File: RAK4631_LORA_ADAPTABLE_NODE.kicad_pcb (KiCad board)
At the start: 2 copper layers, 75 x 49 mm, 20 parts, among them J1 Screw_Terminal_01x03, J10 Conn_01x09_Male, J11 Conn_01x09_Male, J12 Conn_01x09_Male, J14 FBB04004-M40S1003K6M, J2 Screw_Terminal_01x03, J3 Conn_01x03_Male, J4 Conn_01x03_Male, J5 Conn_01x11_Male, J8 Conn_01x11_Male, J9 Conn_01x01_Male

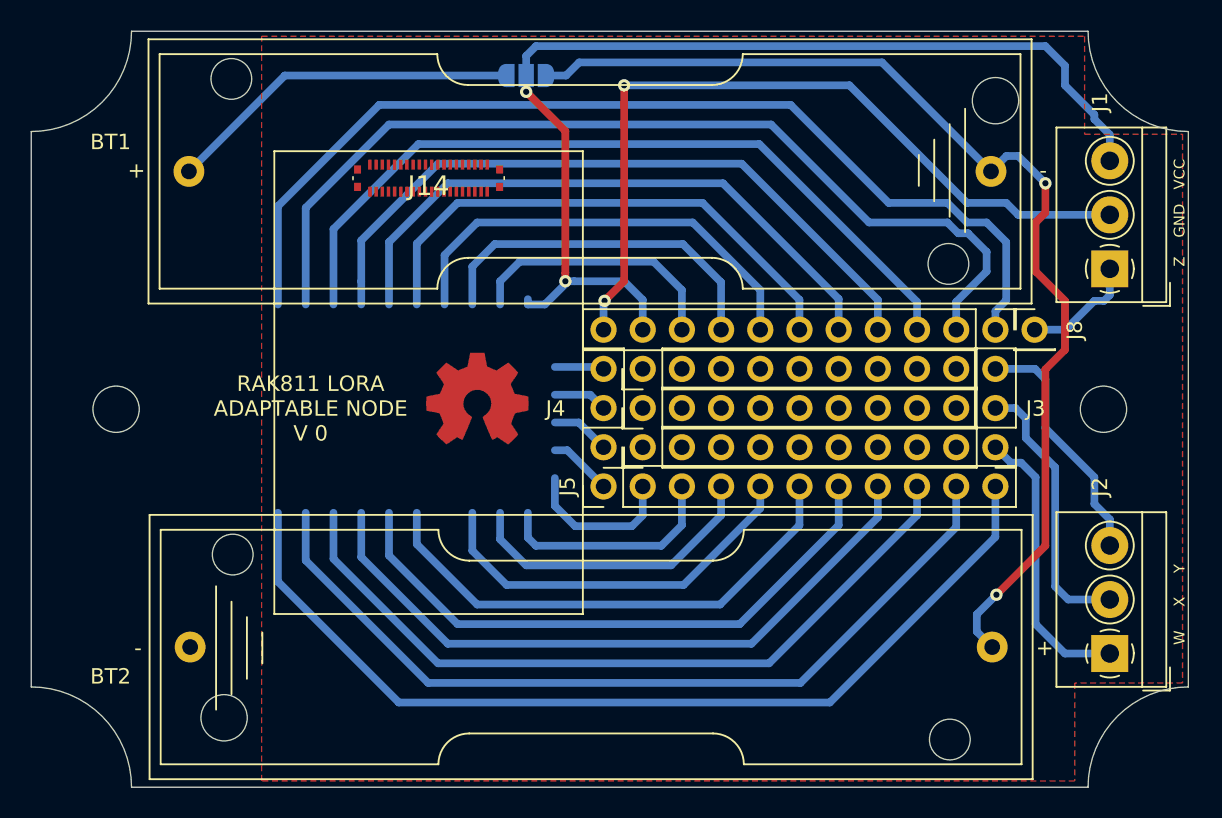
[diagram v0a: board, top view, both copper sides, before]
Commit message: pin assign needs rework
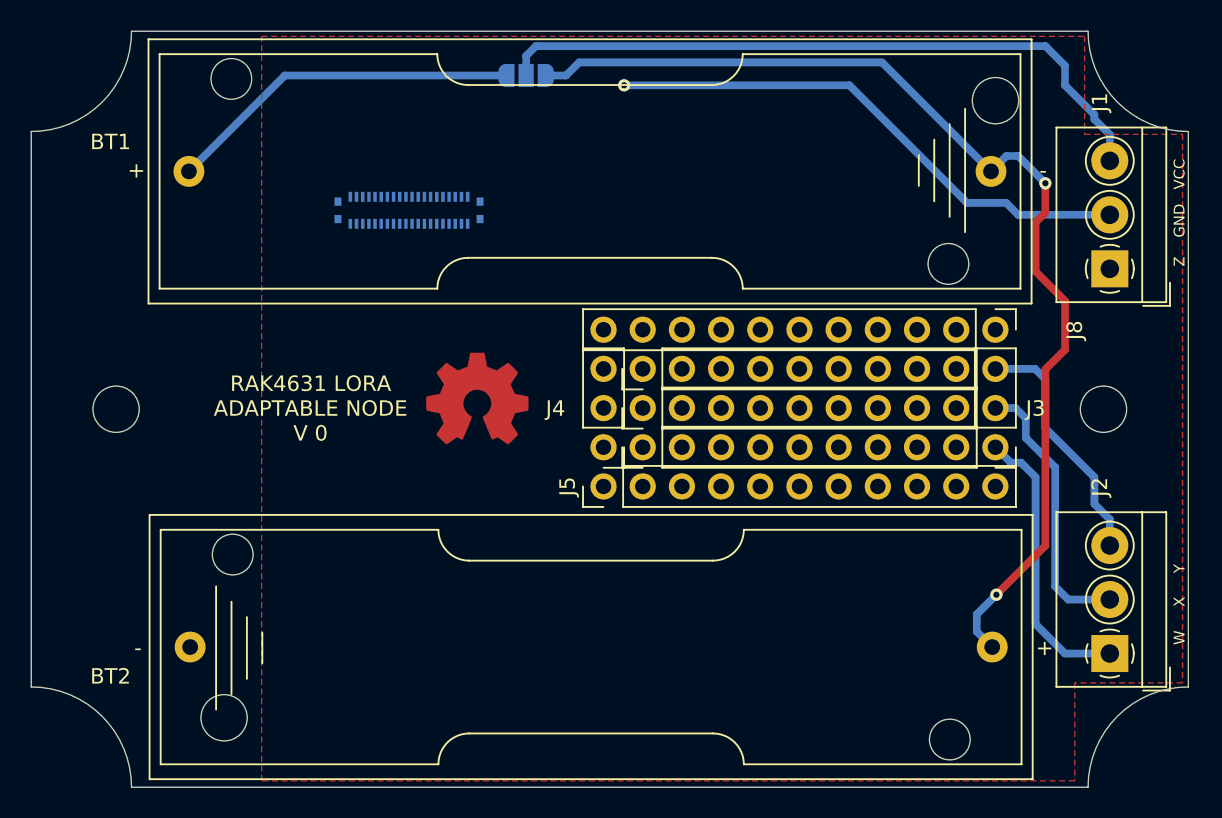
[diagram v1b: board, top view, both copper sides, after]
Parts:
- removed J9: Conn_01x01_Male, Connector_PinHeader_2.54mm:PinHeader_1x01_P2.54mm_Vertical
- J14: moved to B.Cu
- moved J14 2.44 mm to (124.5, 111.6), turned to 180 degrees
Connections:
- J14 pad 18: Net-(J14-Pad18) -> Net-(J14-Pad17)
- J14 pad 2: Net-(J14-Pad2) -> Net-(J14-Pad1)
- J14 pad 3: Net-(J14-Pad3) -> Net-(BT2-Pad2)
- J14 pad 39: Net-(J14-Pad39) -> Net-(BT2-Pad2)
- J14 pad 4: Net-(J14-Pad4) -> Net-(BT2-Pad2)
- J14 pad 40: Net-(J14-Pad40) -> Net-(BT2-Pad2)
- J14 pad 6: Net-(J14-Pad6) -> Net-(J14-Pad5)
- J4 pad 1: Net-(J4-Pad1) -> Net-(J14-Pad32)
- J4 pad 2: Net-(J4-Pad2) -> Net-(J14-Pad30)
- J4 pad 3: Net-(J4-Pad3) -> Net-(J14-Pad28)
- J5 pad 1: Net-(J5-Pad1) -> Net-(J14-Pad34)
- J5 pad 2: Net-(J5-Pad2) -> Net-(J14-Pad33)
- J5 pad 3: Net-(J5-Pad3) -> Net-(J14-Pad31)
- J5 pad 4: Net-(J5-Pad4) -> Net-(J14-Pad29)
- J5 pad 5: Net-(J5-Pad5) -> Net-(J14-Pad27)
- J5 pad 6: Net-(J5-Pad6) -> Net-(J14-Pad25)
- J5 pad 7: Net-(J5-Pad7) -> Net-(J14-Pad21)
- J5 pad 8: Net-(J5-Pad8) -> Net-(J14-Pad19)
- J5 pad 9: Net-(J5-Pad9) -> Net-(J14-Pad13)
- J8 pad 1: Net-(J8-Pad1) -> Net-(J1-Pad1)
- J8 pad 10: Net-(J1-Pad3) -> Net-(J14-Pad22)
- J8 pad 11: Net-(BT2-Pad2) -> Net-(J14-Pad26)
- J8 pad 4: Net-(J8-Pad4) -> Net-(J1-Pad3)
- J8 pad 5: Net-(J8-Pad5) -> Net-(J14-Pad1)
- J8 pad 6: Net-(J8-Pad6) -> Net-(BT2-Pad2)
- J8 pad 7: Net-(J8-Pad7) -> Net-(J14-Pad5)
- J8 pad 8: Net-(J8-Pad8) -> Net-(J14-Pad17)
- J8 pad 9: Net-(J8-Pad9) -> Net-(J14-Pad20)
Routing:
- net Net-(J8-Pad1): track 65.9 -> 0.00 mm
- net Net-(J5-Pad11): track 61.9 -> 0.00 mm
- net Net-(J8-Pad2): track 61.9 -> 0.00 mm
- net Net-(J5-Pad10): track 55.4 -> 0.00 mm
- net Net-(J8-Pad3): track 51.0 -> 0.00 mm
- net Net-(J5-Pad9): track 49.5 -> 0.00 mm
- net Net-(J8-Pad4): track 45.3 -> 0.00 mm
- net Net-(J5-Pad8): track 44.1 -> 0.00 mm
- net Net-(J8-Pad5): track 39.9 -> 0.00 mm
- net Net-(J5-Pad7): track 38.9 -> 0.00 mm
- net Net-(J8-Pad6): track 34.4 -> 0.00 mm
- net Net-(J5-Pad6): track 33.1 -> 0.00 mm
- net Net-(J8-Pad7): track 28.9 -> 0.00 mm
- net Net-(J5-Pad5): track 25.5 -> 0.00 mm
- net Net-(J1-Pad3): track 69.7 -> 44.4 mm, vias 2 -> 0
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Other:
- net class Default: trace_width 0.5 -> 0.2
- net class slimstack added: clearance 0.166, trace_width 0.166, via_dia 0.8, via_drill 0.3
- rule trace_min: 0.2 -> 0.1016
- rule via_min_drill: 0.3 -> 0.2
- board text added: "RAK4631 LORA ADAPTABLE NODE V 0"
- board text removed: "JP2 ANT 1-2 J6 2-3 U.FL"
- board text removed: "RAK811 LORA ADAPTABLE NODE V 0"

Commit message: all elements routed
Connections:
- J4 pad 1: Net-(J14-Pad32) -> Net-(BT2-Pad2)
- J4 pad 2: Net-(J14-Pad30) -> Net-(J14-Pad5)
- J4 pad 3: Net-(J14-Pad28) -> Net-(J14-Pad17)
- J5 pad 1: Net-(J14-Pad34) -> Net-(J14-Pad1)
- J5 pad 10: Net-(J5-Pad10) -> Net-(J14-Pad37)
- J5 pad 2: Net-(J14-Pad33) -> Net-(J14-Pad13)
- J5 pad 3: Net-(J14-Pad31) -> Net-(J14-Pad19)
- J5 pad 4: Net-(J14-Pad29) -> Net-(J14-Pad21)
- J5 pad 5: Net-(J14-Pad27) -> Net-(J14-Pad25)
- J5 pad 6: Net-(J14-Pad25) -> Net-(J14-Pad27)
- J5 pad 7: Net-(J14-Pad21) -> Net-(J14-Pad29)
- J5 pad 8: Net-(J14-Pad19) -> Net-(J14-Pad31)
- J5 pad 9: Net-(J14-Pad13) -> Net-(J14-Pad33)
- J8 pad 11: Net-(J14-Pad26) -> Net-(J14-Pad20)
- J8 pad 3: Net-(J8-Pad3) -> Net-(J1-Pad3)
- J8 pad 4: Net-(J1-Pad3) -> Net-(J14-Pad38)
- J8 pad 5: Net-(J14-Pad1) -> Net-(J14-Pad34)
- J8 pad 6: Net-(BT2-Pad2) -> Net-(J14-Pad32)
- J8 pad 7: Net-(J14-Pad5) -> Net-(J14-Pad30)
- J8 pad 8: Net-(J14-Pad17) -> Net-(J14-Pad28)
- J8 pad 9: Net-(J14-Pad20) -> Net-(J14-Pad26)
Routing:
- net Net-(BT2-Pad2): track 35.0 -> 174.8 mm, vias 1 -> 2
- net Net-(J14-Pad37): track 0.00 -> 76.4 mm
- net Net-(J14-Pad33): track 0.74 -> 70.6 mm
- net Net-(J14-Pad31): track 0.00 -> 63.6 mm
- net Net-(J14-Pad29): track 0.00 -> 58.8 mm
- net Net-(J14-Pad27): track 0.00 -> 53.9 mm
- net Net-(J14-Pad25): track 0.00 -> 48.1 mm
- net Net-(J14-Pad38): track 0.00 -> 47.4 mm
- net Net-(J14-Pad34): track 0.00 -> 43.0 mm
- net Net-(J14-Pad21): track 0.00 -> 41.4 mm
- net Net-(J14-Pad32): track 0.00 -> 39.5 mm
- net Net-(J14-Pad19): track 0.00 -> 36.7 mm
- net Net-(J14-Pad30): track 0.00 -> 36.1 mm
- net Net-(J14-Pad28): track 0.18 -> 33.4 mm
- net Net-(J14-Pad13): track 0.00 -> 32.6 mm
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- added copper zone on B.Cu, net Net-(BT2-Pad2)
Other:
- net class Default: trace_width 0.2 -> 0.5
- net class slimstack: clearance 0.166 -> 0.1778; via_drill 0.3 -> 0.4
- rule trace_min: 0.1016 -> 0.15
